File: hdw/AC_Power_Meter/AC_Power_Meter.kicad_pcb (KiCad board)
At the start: 2 copper layers, 261 parts, among them J1001 USB_B_Mini, J201 HT_IN, J202 NEUT_IN, J203 EARTH_IN, J401 HT_OUT, J402 NEUT_OUT, J403 EARTH_OUT, J501 AUX_IN, J801 Prog, SW1702 MRESET, SW1703 SW_Toggle, U1001 LT6700-1-S6, U1002 FT234XD, U1003 74LVC1G06, U1004 TPD3S014DBVR, U1201 SSD1306, U1402 74LVC1G17, U1501 74LVC1G32, U1502 FOD4218, U1601 74LVC1G06, U1602 74LVC1G06, U1603 74LVC1G06, U1604 74LVC1G06, U1605 74LVC1G06, U1606 74LVC1G06, U1607 74LVC1G06, U1701 TLC555CPS, U1702 TLC555CPS, U301 ACS722LLCTR-20AB, U501 LT6700-1-S6, U502 74LVC1G17, U601 74LVC1G17, U602 LT3973-DD, U701 PIC18LF67K40-I/PT, U801 TL331, U802 74LVC1G86

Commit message: Arranged a few pages of components
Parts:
- added J1701: Ext_SW_Toggle, Pin_Headers:Pin_Header_Straight_1x02_Pitch2.54mm, F.Cu at (96.9, 20.1)
- added Q1501: BT139-600, TO_SOT_Packages_THT:TO-220-3_Vertical, F.Cu at (144.4, 55.2)
- added U1101: ISO7321C, Housings_SOIC:SOIC-8_3.9x4.9mm_Pitch1.27mm, F.Cu at (249.0, 31.2)
- added U1401: LTV-356T, Housings_SOIC:SO-4_4.4x3.6mm_Pitch2.54mm, F.Cu at (205.1, 67.4)
- added U901: LTC6240IS5, TO_SOT_Packages_SMD:SOT-23-5, F.Cu at (39.3, 81.3)
- added U902: LTC6240IS5, TO_SOT_Packages_SMD:SOT-23-5, F.Cu at (39.3, 85.0)
- added U903: LTC6240IS5, TO_SOT_Packages_SMD:SOT-23-5, F.Cu at (43.1, 81.3)
- added U904: LTC6240IS5, TO_SOT_Packages_SMD:SOT-23-5, F.Cu at (43.1, 85.0)
- added X701: ASV-16.000MHz, Oscillators:Oscillator_SMD_Abracon_ASV-4pin_7.0x5.1mm, F.Cu at (216.8, 29.0)
- C1001, C1002, C1003, C1004, C1005, C1006, C1008, C1009, C1010, C1011, C1101, C1103, C1402, C301, C302, C303, R1001, R1002, R1003, R1004, R1005, R1007, R1008, R1101, R1102, R1404, R705, U1001, U1002: moved to B.Cu
- moved C802 174.7 mm to (263.3, 118.4)
- moved C803 174.7 mm to (266.1, 114.9)
- moved C804 174.7 mm to (270.4, 110.7)
- moved C805 174.7 mm to (263.3, 117.0)
- moved C806 174.7 mm to (263.3, 115.7)
- moved C807 174.7 mm to (267.1, 113.5)
- moved C808 174.7 mm to (263.3, 114.3)
- moved J801 174.7 mm to (251.3, 111.8)
- moved L801 174.7 mm to (266.0, 116.4)
- moved L802 174.7 mm to (263.2, 119.9)
- moved R801 174.7 mm to (273.1, 110.7)
- moved R803 174.7 mm to (268.8, 114.9)
- moved R805 174.7 mm to (263.1, 121.4)
- moved R806 174.7 mm to (272.7, 113.6)
- moved R807 174.7 mm to (263.1, 122.9)
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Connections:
- R705 pad 2: (no net) -> Net-(R705-Pad2)
- R905 pad 2: (no net) -> Net-(R905-Pad2)
- R906 pad 1: (no net) -> Net-(R906-Pad1)
- R908 pad 2: (no net) -> Net-(R908-Pad2)
- U701 pad 39: (no net) -> CLKIN
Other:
- board text added: "AC OUT"
- board text added: "Current Sensor"
- board text added: "Micro"
- board text added: "OLED"
- board text added: "USB"
- board text added: "ZCD"

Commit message: Nailed down board outline, placed a few sections
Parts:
- removed MH1304: MountingHole, Mounting_Holes:MountingHole_3mm_Pad_Via
- added D901: 1N4148WS, Diodes_SMD:D_SOD-323, F.Cu at (288.2, 124.6)
- added Q1701: 2N7002, TO_SOT_Packages_SMD:SOT-23, F.Cu at (437.5, 62.1)
- added Q501: DMP3099L-7, TO_SOT_Packages_SMD:SOT-23, F.Cu at (86.2, -49.1)
- C1502, C1701, C1702, C1703, C1704, C501, C502, C503, C504, C604, C607, C802, C803, C804, C805, C808, C901, C902, C903, C904, C905, C906, C907, C908, C909, C910, C911, C912, C913, C914, C915, C917, C918, C919, C920, C921, F201, F501, L801, L802, R1501, R1502, R1506, R1601, R1602, R1605, R1606, R1609, R1610, R1613, R1701, R1702, R301, R302, R507, R508, R601, R605, R606, R802, R803, R805, R806, R807, R907, U301, Z501: moved to B.Cu
- C301, C302, C303: moved to F.Cu
- MH1301, MH1302, MH1303, MH1305, MH1306, MH1307, MH1308: footprint Mounting_Holes:MountingHole_3mm_Pad_Via -> Mounting_Holes:MountingHole_3mm
- moved R501 426.9 mm to (447.4, 76.7)
- moved R502 426.9 mm to (444.8, 76.7)
- moved C1502 375.1 mm to (494.0, 163.1)
- moved Q1501 372.8 mm to (501.4, 162.6), turned to 90 degrees
- moved R1506 364.9 mm to (494.0, 159.1), turned to 180 degrees
- moved U1502 364.7 mm to (484.6, 161.8)
- moved R1504 364.2 mm to (494.0, 164.3)
- moved R1505 363.8 mm to (494.0, 159.1)
- moved U1501 353.4 mm to (476.1, 160.3)
- moved R1503 345.4 mm to (478.7, 160.1), turned to 270 degrees
- moved C1501 344.6 mm to (476.1, 162.4), turned to 180 degrees
- moved R1502 343.7 mm to (476.1, 160.9)
- moved R1501 342.2 mm to (476.1, 159.4)
- moved R1705 322.0 mm to (442.2, 60.3)
- moved R1706 322.0 mm to (442.2, 61.8)
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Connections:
- J501 pad 1: (no net) -> Net-(J501-Pad1)
- J501 pad 3: (no net) -> GND
- R1706 pad 1: (no net) -> Net-(Q1701-Pad1)
- U903 pad 1: (no net) -> Net-(D901-Pad2)
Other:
- board outline added: 100 x 100 mm
- board text added: "LEDs"
- board text added: "Signal Conditioning"
- board text added: "Switches"
- board text added: "TRIAC"
- board text removed: "AC OUT"

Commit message: Placed a lot more parts, netlist cleanup
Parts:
- C301, C302, C303, C704, C705, C706, R1705, Z801: moved to B.Cu
- R301, R302, U301: moved to F.Cu
- moved Q1501 400.3 mm to (102.7, 125.9), turned to 0 degrees
- moved R1504 395.7 mm to (101.0, 118.5), turned to 270 degrees
- moved C1502 394.3 mm to (102.2, 118.5), turned to 270 degrees
- moved R1505 390.0 mm to (106.2, 118.5), turned to 270 degrees
- moved R1506 390.0 mm to (106.2, 118.5), turned to 90 degrees
- moved R501 388.9 mm to (58.8, 91.3)
- moved R502 388.9 mm to (56.2, 91.3)
- moved R602 388.9 mm to (63.1, 89.0)
- moved R603 388.9 mm to (61.3, 86.1)
- moved R701 388.9 mm to (56.5, 84.6)
- moved R702 388.9 mm to (56.5, 83.1)
- moved R703 388.9 mm to (52.8, 80.5)
- moved R704 388.9 mm to (59.4, 80.4)
- moved U1502 384.8 mm to (103.5, 109.1), turned to 270 degrees
- moved C1501 378.3 mm to (102.9, 100.6), turned to 90 degrees
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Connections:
- MH1301 pad 1: Earth_Protective -> (no net)
- MH1302 pad 1: Earth_Protective -> (no net)
- MH1303 pad 1: Earth_Protective -> (no net)
- MH1305 pad 1: Earth_Protective -> (no net)
- MH1306 pad 1: Earth_Protective -> (no net)
- MH1307 pad 1: Earth_Protective -> (no net)
- MH1308 pad 1: Earth_Protective -> (no net)
- R1705 pad 1: Net-(R1705-Pad1) -> Net-(Q1701-Pad1)
- R1706 pad 2: Net-(R1705-Pad1) -> Net-(R1706-Pad2)
- U1201 pad 1: GND -> +3V3
- U1201 pad 2: +3V3 -> GND
- U1701 pad 3: Net-(R1705-Pad1) -> Net-(R1706-Pad2)
- U301 pad 1: HT -> ISNS_HT_OUT
- U301 pad 2: HT -> ISNS_HT_OUT
- U301 pad 3: ISNS_HT_OUT -> HT
- U301 pad 4: ISNS_HT_OUT -> HT
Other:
- board text removed: "Current Sensor"
- board text removed: "Micro"
- board text removed: "OLED"
- board text removed: "Signal Conditioning"
- board text removed: "Switches"
- board text removed: "TRIAC"
- board text removed: "USB"
- board text removed: "ZCD"

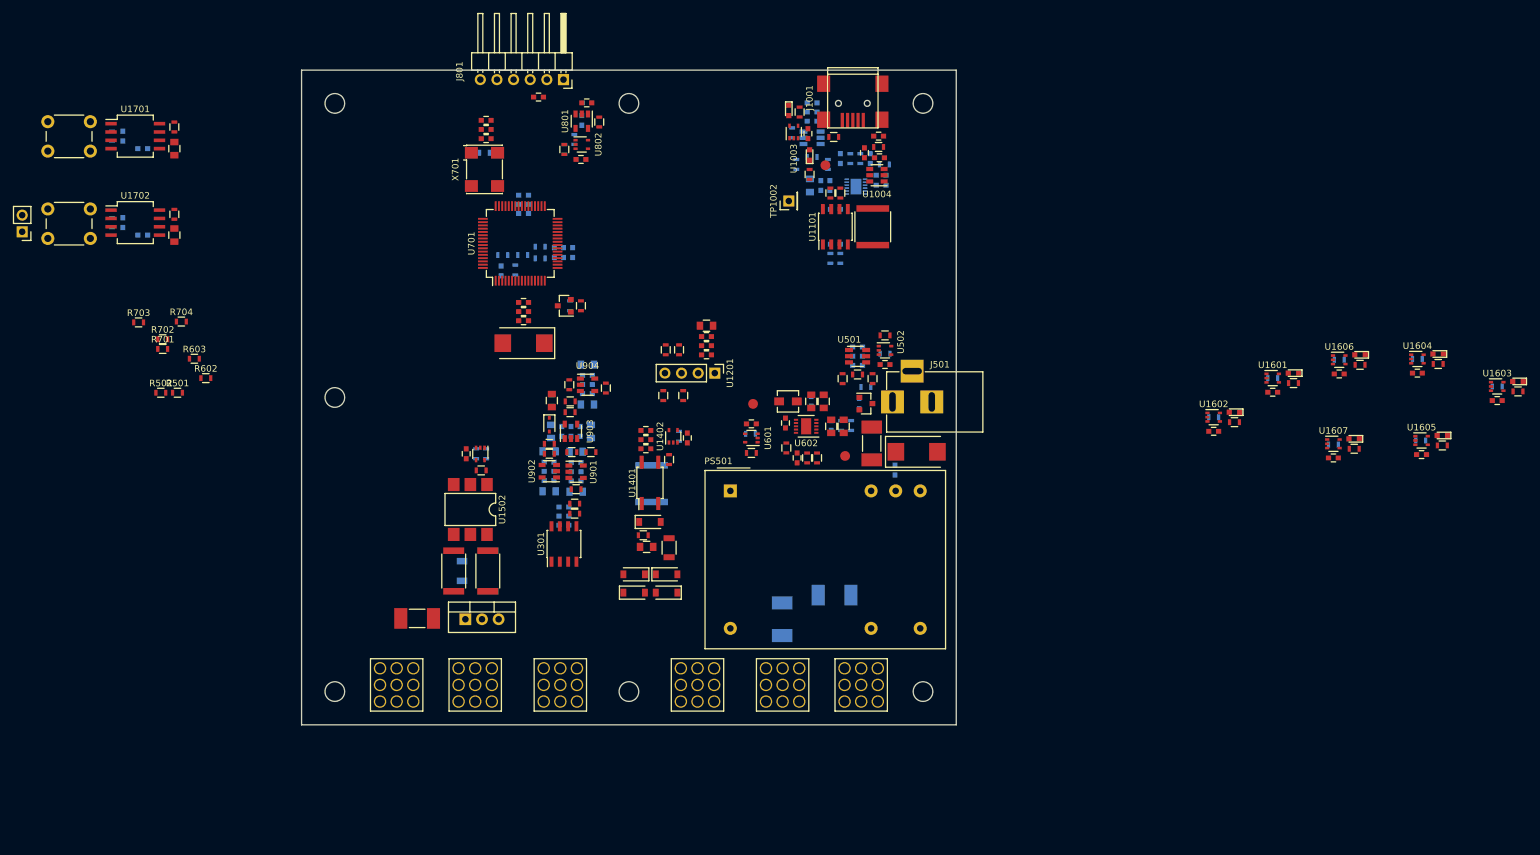
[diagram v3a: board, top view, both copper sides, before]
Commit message: Finished placing parts
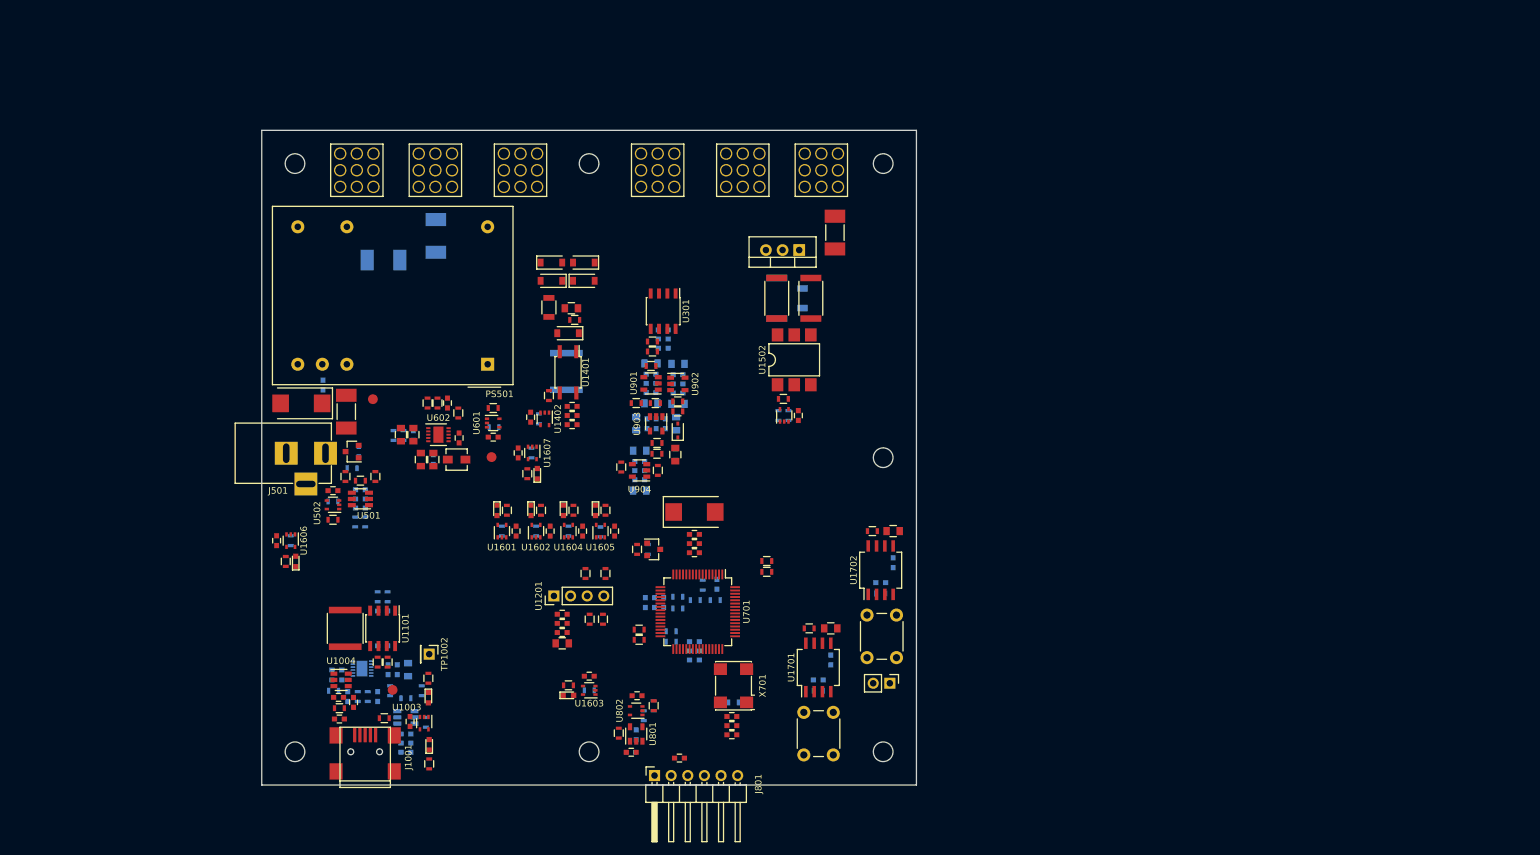
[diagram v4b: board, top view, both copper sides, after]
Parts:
- R501, R502, R703, R704: moved to B.Cu
- moved R1612 166.8 mm to (75.3, 117.0), turned to 90 degrees
- moved D1606 165.6 mm to (76.8, 117.0), turned to 90 degrees
- moved C1606 164.3 mm to (73.9, 113.9), turned to 90 degrees
- moved R1610 162.5 mm to (76.1, 113.9), turned to 270 degrees
- moved U1606 162.5 mm to (76.1, 113.9), turned to 270 degrees
- moved D1603 152.8 mm to (118.5, 137.5), turned to 0 degrees
- moved R1607 151.8 mm to (118.5, 136.0), turned to 0 degrees
- moved J1701 149.4 mm to (167.6, 135.6), turned to 270 degrees
- moved R1605 146.2 mm to (121.7, 136.7), turned to 180 degrees
- moved U1603 146.2 mm to (121.7, 136.7), turned to 180 degrees
- moved C1603 144.9 mm to (121.7, 134.6), turned to 0 degrees
- moved SW1702 142.2 mm to (158.9, 140.1), turned to 270 degrees
- moved MH1303 137.9 mm to (76.7, 146.1), turned to 180 degrees
- moved R1701 137.2 mm to (156.7, 136.8), turned to 180 degrees
- moved SW1703 135.9 mm to (168.6, 125.2), turned to 270 degrees
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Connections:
- U701 pad 31: (no net) -> Net-(R701-Pad2)
- U701 pad 32: (no net) -> Net-(R702-Pad1)
- U701 pad 49: Net-(R702-Pad1) -> (no net)
- U701 pad 50: Net-(R701-Pad2) -> (no net)
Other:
- board text removed: "LEDs"

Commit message: Added some PCB design rules
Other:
- net class Default: clearance 0.2 -> 0.127; trace_width 0.25 -> 0.1016
- net class Power added: clearance 0.127, trace_width 0.635, via_dia 0.8, via_drill 0.4
- net class Power_HV added: clearance 1.27, trace_width 1.27, via_dia 0.8, via_drill 0.4
- net class Signal added: clearance 0.127, trace_width 0.1016, via_dia 0.5, via_drill 0.25
- net class Signal_HV added: clearance 1.27, trace_width 0.508, via_dia 0.8, via_drill 0.4
- rule trace_clearance: 0.2 -> 0.127
- rule trace_min: 0.2 -> 0.0889
- rule via_min_drill: 0.3 -> 0.2
- rule via_min_size: 0.4 -> 0.45
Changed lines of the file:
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@@
   )
   (setup
-    (last_trace_width 0.25)
-    (trace_clearance 0.2)
+    (last_trace_width 0.1016)
+    (trace_clearance 0.127)
     (zone_clearance 0.508)
     (zone_45_only no)
-    (trace_min 0.2)
+    (trace_min 0.0889)
     (segment_width 0.2)
     (edge_width 0.15)
     (via_size 0.8)
     (via_drill 0.4)
-    (via_min_size 0.4)
-    (via_min_drill 0.3)
+    (via_min_size 0.45)
+    (via_min_drill 0.2)
     (uvia_size 0.3)
     (uvia_drill 0.1)
@@
   (net 121 "Net-(R1706-Pad2)")
   (net_class Default "This is the default net class."
-    (clearance 0.2)
-    (trace_width 0.25)
+    (clearance 0.127)
+    (trace_width 0.1016)
     (via_dia 0.8)
     (via_drill 0.4)
     (uvia_dia 0.3)
     (uvia_drill 0.1)
-    (add_net +0.825V_REF)
-    (add_net +12V)
-    (add_net +3.3VADC)
-    (add_net +3V3)
-    (add_net +5V_USB)
-    (add_net "/USB UART Bridge/BRIDGE_USB+")
-    (add_net "/USB UART Bridge/BRIDGE_USB-")
-    (add_net "/USB UART Bridge/CONN_USB+")
-    (add_net "/USB UART Bridge/CONN_USB-")
-    (add_net ADC_Error)
-    (add_net CLKIN)
-    (add_net Comm_Error)
-    (add_net Earth_Protective)
-    (add_net GND)
-    (add_net GNDA)
-    (add_net GNDPWR)
-    (add_net GND_USB)
-    (add_net HT)
-    (add_net Heartbeat)
-    (add_net I2C_SCL)
-    (add_net I2C_SDA)
-    (add_net ICSPCLK)
-    (add_net ICSPDAT)
-    (add_net ICSP_DETECT)
-    (add_net ISNS_ADC)
-    (add_net ISNS_HT_OUT)
-    (add_net ISNS_OUT)
-    (add_net NEUT)
-    (add_net "Net-(C1004-Pad1)")
-    (add_net "Net-(C1009-Pad1)")
-    (add_net "Net-(C1013-Pad1)")
-    (add_net "Net-(C1014-Pad1)")
-    (add_net "Net-(C1401-Pad1)")
-    (add_net "Net-(C1401-Pad2)")
-    (add_net "Net-(C1502-Pad1)")
-    (add_net "Net-(C1701-Pad1)")
-    (add_net "Net-(C1702-Pad1)")
-    (add_net "Net-(C1705-Pad1)")
-    (add_net "Net-(C1706-Pad1)")
-    (add_net "Net-(C605-Pad1)")
-    (add_net "Net-(C605-Pad2)")
-    (add_net "Net-(C606-Pad2)")
-    (add_net "Net-(C801-Pad1)")
-    (add_net "Net-(C808-Pad1)")
-    (add_net "Net-(C916-Pad1)")
-    (add_net "Net-(D1001-Pad1)")
-    (add_net "Net-(D1002-Pad1)")
-    (add_net "Net-(D1405-Pad1)")
-    (add_net "Net-(D1601-Pad1)")
-    (add_net "Net-(D1602-Pad1)")
-    (add_net "Net-(D1603-Pad1)")
-    (add_net "Net-(D1604-Pad1)")
-    (add_net "Net-(D1605-Pad1)")
-    (add_net "Net-(D1606-Pad1)")
-    (add_net "Net-(D1607-Pad1)")
-    (add_net "Net-(D901-Pad2)")
-    (add_net "Net-(F201-Pad2)")
-    (add_net "Net-(F401-Pad1)")
-    (add_net "Net-(F501-Pad1)")
-    (add_net "Net-(F502-Pad2)")
     (add_net "Net-(J1001-Pad6)")
     (add_net "Net-(J1701-Pad2)")
@@
     (add_net ~USB_ACTIVE)
   )
+  (net_class Power ""
+    (clearance 0.127)
+    (trace_width 0.635)
+    (via_dia 0.8)
+    (via_drill 0.4)
+    (uvia_dia 0.3)
+    (uvia_drill 0.1)
+    (add_net +0.825V_REF)
+    (add_net +12V)
+    (add_net +3.3VADC)
+    (add_net +3V3)
+    (add_net +5V_USB)
+    (add_net GND)
+    (add_net GNDA)
+    (add_net GNDPWR)
+    (add_net GND_USB)
+    (add_net "Net-(C1013-Pad1)")
+    (add_net "Net-(C1014-Pad1)")
+    (add_net "Net-(C605-Pad2)")
+    (add_net "Net-(F502-Pad2)")
+  )
+  (net_class Power_HV ""
+    (clearance 1.27)
+    (trace_width 1.27)
+    (via_dia 0.8)
+    (via_drill 0.4)
+    (uvia_dia 0.3)
+    (uvia_drill 0.1)
+    (add_net Earth_Protective)
+    (add_net HT)
+    (add_net ISNS_HT_OUT)
+    (add_net NEUT)
+    (add_net "Net-(F201-Pad2)")
+    (add_net "Net-(F401-Pad1)")
+    (add_net "Net-(F501-Pad1)")
+  )
+  (net_class Signal ""
+    (clearance 0.127)
+    (trace_width 0.1016)
+    (via_dia 0.5)
+    (via_drill 0.25)
+    (uvia_dia 0.3)
+    (uvia_drill 0.1)
+    (add_net "/USB UART Bridge/BRIDGE_USB+")
+    (add_net "/USB UART Bridge/BRIDGE_USB-")
+    (add_net "/USB UART Bridge/CONN_USB+")
+    (add_net "/USB UART Bridge/CONN_USB-")
+    (add_net ADC_Error)
+    (add_net CLKIN)
+    (add_net Comm_Error)
+    (add_net Heartbeat)
+    (add_net I2C_SCL)
+    (add_net I2C_SDA)
+    (add_net ICSPCLK)
+    (add_net ICSPDAT)
+    (add_net ICSP_DETECT)
+    (add_net ISNS_ADC)
+    (add_net ISNS_OUT)
+    (add_net "Net-(C1004-Pad1)")
+    (add_net "Net-(C1009-Pad1)")
+    (add_net "Net-(C1701-Pad1)")
+    (add_net "Net-(C1702-Pad1)")
+    (add_net "Net-(C1705-Pad1)")
+    (add_net "Net-(C1706-Pad1)")
+    (add_net "Net-(C605-Pad1)")
+    (add_net "Net-(C606-Pad2)")
+    (add_net "Net-(C801-Pad1)")
+    (add_net "Net-(C808-Pad1)")
+    (add_net "Net-(C916-Pad1)")
+    (add_net "Net-(D1001-Pad1)")
+    (add_net "Net-(D1002-Pad1)")
+    (add_net "Net-(D1601-Pad1)")
+    (add_net "Net-(D1602-Pad1)")
+    (add_net "Net-(D1603-Pad1)")
+    (add_net "Net-(D1604-Pad1)")
+    (add_net "Net-(D1605-Pad1)")
+    (add_net "Net-(D1606-Pad1)")
+    (add_net "Net-(D1607-Pad1)")
+    (add_net "Net-(D901-Pad2)")
+  )
+  (net_class Signal_HV ""
+    (clearance 1.27)
+    (trace_width 0.508)
+    (via_dia 0.8)
+    (via_drill 0.4)
+    (uvia_dia 0.3)
+    (uvia_drill 0.1)
+    (add_net "Net-(C1401-Pad1)")
+    (add_net "Net-(C1401-Pad2)")
+    (add_net "Net-(C1502-Pad1)")
+    (add_net "Net-(D1405-Pad1)")
+  )
   (module Mounting_Holes:MountingHole_3mm locked (layer F.Cu)
